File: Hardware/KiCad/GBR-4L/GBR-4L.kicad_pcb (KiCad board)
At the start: 4 copper layers, 160 x 100 mm, 188 parts, among them J1 USB4105-GF-A, J101 EM7565 M.2 Key B socket, J102 MODEM_CONTROL, J201 EM7565 M.2 Key B socket, J202 MODEM_CONTROL, J301 EM7565 M.2 Key B socket, J302 MODEM_CONTROL, J401 EM7565 M.2 Key B socket, J402 MODEM_CONTROL, J511 2452808-1 nano-SIM, J521 2452808-1 nano-SIM, J531 2452808-1 nano-SIM, J541 2452808-1 nano-SIM, J701 12V INPUT 5A, Q701 30V P-MOSFET low-RDS(on), Q911 MMBT3906, Q921 MMBT3906, Q931 MMBT3906, Q941 MMBT3906, SW911 MODEM 1 RESET, SW912 MODEM 1 RF DISABLE, SW921 MODEM 2 RESET, SW922 MODEM 2 RF DISABLE, SW931 MODEM 3 RESET, SW932 MODEM 3 RF DISABLE, SW941 MODEM 4 RESET, SW942 MODEM 4 RF DISABLE, U1 USBLC6-2SC6, U11 LOW-CAP SIM ESD ARRAY, U12 LOW-CAP SIM ESD ARRAY, U13 LOW-CAP SIM ESD ARRAY, U14 LOW-CAP SIM ESD ARRAY, U2 USB2514Bi-I/M2, U21 TPS56339DDCR, U22 TPS56339DDCR, U23 TPS56339DDCR, U24 TPS56339DDCR, U25 TPS56339DDCR, Y1 24MHz

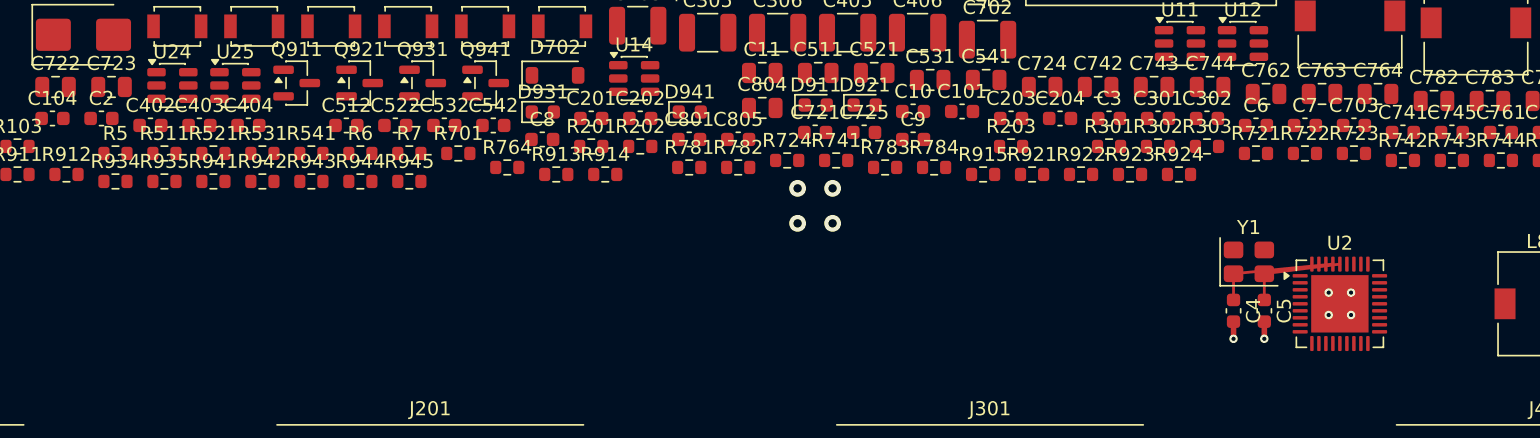
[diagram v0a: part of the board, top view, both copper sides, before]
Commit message: Place and route USB hub filters
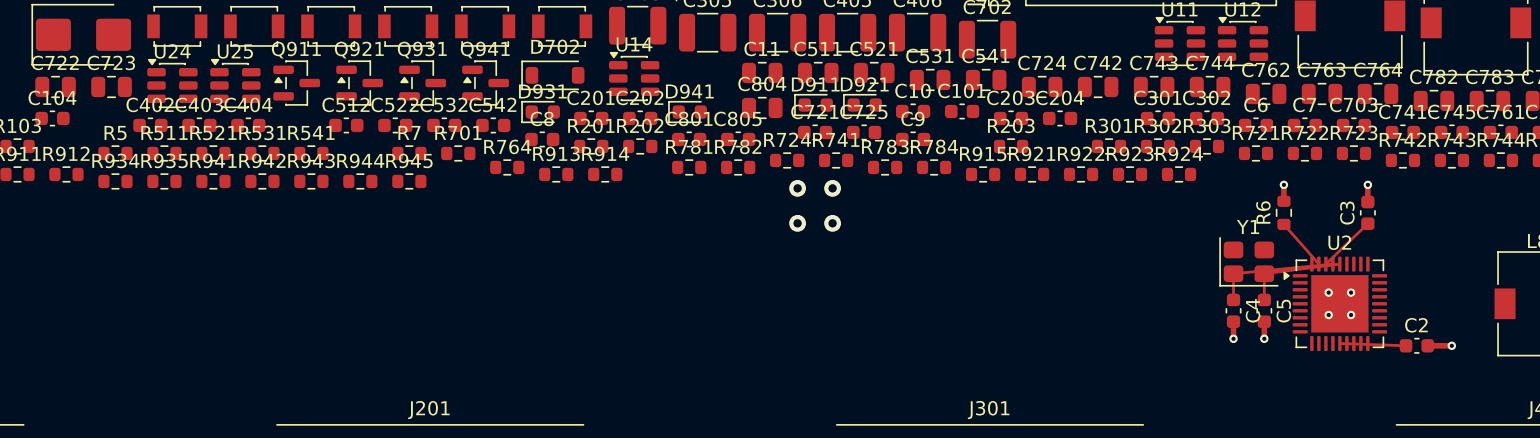
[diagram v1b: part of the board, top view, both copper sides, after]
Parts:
- moved C2 95.4 mm to (150.5, 58.0)
- moved R6 66.1 mm to (141.0, 48.5), turned to 90 degrees
- moved C3 19.7 mm to (147.0, 48.5), turned to 90 degrees
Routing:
- net HUB_CRFILT: track 0.00 -> 4.73 mm
- net HUB_PLLFILT: track 0.00 -> 4.16 mm
- net GND: track 18.0 -> 22.1 mm, vias 57 -> 60
- net HUB_RBIAS: track 0.00 -> 3.78 mm
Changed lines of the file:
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@@
 	(footprint "Capacitor_SMD:C_0603_1608Metric"
 		(layer "F.Cu")
-		(at 56.505 41.754999)
+		(at 150.5 58)
 		(descr "Capacitor SMD 0603 (1608 Metric), square (rectangular) end terminal, IPC-7351 nominal, (Body size source: IPC-SM-782 page 76, https://www.pcb-3d.com/wordpress/wp-content/uploads/ipc-sm-782a_amendment_1_and_2.pdf)")
 		(tags "capacitor")
@@
 	(footprint "Resistor_SMD:R_0603_1608Metric"
 		(layer "F.Cu")
-		(at 75.005 44.255)
+		(at 141 48.5 90)
 		(descr "Resistor SMD 0603 (1608 Metric), square (rectangular) end terminal, IPC-7351 nominal, (Body size source: IPC-SM-782 page 72, https://www.pcb-3d.com/wordpress/wp-content/uploads/ipc-sm-782a_amendment_1_and_2.pdf)")
 		(tags "resistor")
 		(property "Reference" "R6"
-			(at 0 -1.43 0)
+			(at 0 -1.43 90)
 			(layer "F.SilkS")
 			(effects
@@
 		)
 		(property "Value" "12.0k 1%"
-			(at 0 1.43 0)
+			(at 0 1.43 90)
 			(layer "F.Fab")
 			(effects
@@
 		)
 		(property "Datasheet" ""
-			(at 0 0 0)
+			(at 0 0 90)
 			(layer "F.Fab")
 			(hide yes)
@@
 		)
 		(property "Description" ""
-			(at 0 0 0)
+			(at 0 0 90)
 			(layer "F.Fab")
 			(hide yes)
@@
 		)
 		(property "KiLib_Generator" "SMD_2terminal_chip_molded"
-			(at 0 0 0)
+			(at 0 0 90)
 			(layer "F.SilkS")
 			(hide yes)
@@
 		)
 		(fp_text user "${REFERENCE}"
-			(at 0 0 0)
+			(at 0 0 90)
 			(layer "F.Fab")
 			(effects
@@
 		)
 		(pad "1" smd roundrect
-			(at -0.825 0)
+			(at -0.825 0 90)
 			(size 0.8 0.95)
 			(layers "F.Cu" "F.Mask" "F.Paste")
@@
 		)
 		(pad "2" smd roundrect
-			(at 0.825 0)
+			(at 0.825 0 90)
 			(size 0.8 0.95)
 			(layers "F.Cu" "F.Mask" "F.Paste")
@@
 	(footprint "Capacitor_SMD:C_0603_1608Metric"
 		(layer "F.Cu")
-		(at 128.504999 41.754999)
+		(at 147 48.5 90)
 		(descr "Capacitor SMD 0603 (1608 Metric), square (rectangular) end terminal, IPC-7351 nominal, (Body size source: IPC-SM-782 page 76, https://www.pcb-3d.com/wordpress/wp-content/uploads/ipc-sm-782a_amendment_1_and_2.pdf)")
 		(tags "capacitor")
 		(property "Reference" "C3"
-			(at 0 -1.43 0)
+			(at 0 -1.43 90)
 			(layer "F.SilkS")
 			(effects
@@
 		)
 		(property "Value" "100nF"
-			(at 0 1.43 0)
+			(at 0 1.43 90)
 			(layer "F.Fab")
 			(effects
@@
 		)
 		(property "Datasheet" ""
-			(at 0 0 0)
+			(at 0 0 90)
 			(layer "F.Fab")
 			(hide yes)
@@
 		)
 		(property "Description" ""
-			(at 0 0 0)
+			(at 0 0 90)
 			(layer "F.Fab")
 			(hide yes)
@@
 		)
 		(property "KiLib_Generator" "SMD_2terminal_chip_molded"
-			(at 0 0 0)
+			(at 0 0 90)
 			(layer "F.SilkS")
 			(hide yes)
@@
 		)
 		(fp_text user "${REFERENCE}"
-			(at 0 0 0)
+			(at 0 0 90)
 			(layer "F.Fab")
 			(effects
@@
 		)
 		(pad "1" smd roundrect
-			(at -0.775 0)
+			(at -0.775 0 90)
 			(size 0.9 0.95)
 			(layers "F.Cu" "F.Mask" "F.Paste")
@@
 		)
 		(pad "2" smd roundrect
-			(at 0.775 0)
+			(at 0.775 0 90)
 			(size 0.9 0.95)
 			(layers "F.Cu" "F.Mask" "F.Paste")
@@
 	)
 	(segment
+		(start 147 47.725)
+		(end 147 46.5)
+		(width 0.4)
+		(layer "F.Cu")
+		(net "GND")
+	)
+	(segment
+		(start 151.275 58)
+		(end 153 58)
+		(width 0.4)
+		(layer "F.Cu")
+		(net "GND")
+	)
+	(segment
 		(start 171.32 31.8)
 		(end 168.5 31.8)
@@
 		(net "GND")
 	)
+	(segment
+		(start 141 47.675)
+		(end 141 46.5)
+		(width 0.4)
+		(layer "F.Cu")
+		(net "GND")
+	)
 	(via
 		(at 168.5 31.8)
@@
 	)
 	(via
+		(at 153 58)
+		(size 0.6)
+		(drill 0.3)
+		(layers "F.Cu" "B.Cu")
+		(net "GND")
+	)
+	(via
 		(at 139.6 57.5)
 		(size 0.6)
@@
 	)
 	(via
+		(at 147 46.5)
+		(size 0.6)
+		(drill 0.3)
+		(layers "F.Cu" "B.Cu")
+		(net "GND")
+	)
+	(via
 		(at 110 117)
 		(size 0.6)
@@
 	)
 	(via
+		(at 141 46.5)
+		(size 0.6)
+		(drill 0.3)
+		(layers "F.Cu" "B.Cu")
+		(net "GND")
+	)
+	(via
 		(at 170.325 56)
 		(size 0.6)
@@
 	)
 	(segment
+		(start 149.725 58)
+		(end 145 57.8375)
+		(width 0.2)
+		(layer "F.Cu")
+		(net "HUB_CRFILT")
+	)
+	(segment
 		(start 171.9 39.32)
 		(end 168.5 39.32)
@@
 	)
 	(segment
+		(start 141 49.325)
+		(end 143.5 52.1625)
+		(width 0.2)
+		(layer "F.Cu")
+		(net "HUB_RBIAS")
+	)
+	(segment
 		(start 137.4 52.85)
 		(end 137.4 54.725)
@@
 		(net "HUB_XTALIN")
 	)
+	(segment
+		(start 147 49.275)
+		(end 144 52.1625)
+		(width 0.2)
+		(layer "F.Cu")
+		(net "HUB_PLLFILT")
+	)
 	(zone

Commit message: Place and route USB hub decoupling
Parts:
- moved C8 64.0 mm to (151.5, 51.5)
- moved C11 49.7 mm to (148.0, 61.0), turned to -90 degrees
- moved C9 35.3 mm to (145.0, 61.0), turned to -90 degrees
- moved C10 33.9 mm to (142.0, 61.0), turned to -90 degrees
- moved C7 14.8 mm to (151.5, 54.0)
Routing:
- net +3V3_SYS: track 0.00 -> 17.4 mm
- net GND: track 22.1 -> 29.0 mm, vias 60 -> 65
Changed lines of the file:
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@@
 	(footprint "Capacitor_SMD:C_0603_1608Metric"
 		(layer "F.Cu")
-		(at 88.005001 43.254999)
+		(at 151.5 51.5)
 		(descr "Capacitor SMD 0603 (1608 Metric), square (rectangular) end terminal, IPC-7351 nominal, (Body size source: IPC-SM-782 page 76, https://www.pcb-3d.com/wordpress/wp-content/uploads/ipc-sm-782a_amendment_1_and_2.pdf)")
 		(tags "capacitor")
@@
 	(footprint "Capacitor_SMD:C_0603_1608Metric"
 		(layer "F.Cu")
-		(at 114.505 41.254999)
+		(at 142 61 -90)
 		(descr "Capacitor SMD 0603 (1608 Metric), square (rectangular) end terminal, IPC-7351 nominal, (Body size source: IPC-SM-782 page 76, https://www.pcb-3d.com/wordpress/wp-content/uploads/ipc-sm-782a_amendment_1_and_2.pdf)")
 		(tags "capacitor")
 		(property "Reference" "C10"
-			(at 0 -1.43 0)
+			(at 0 -1.43 270)
 			(layer "F.SilkS")
 			(effects
@@
 		)
 		(property "Value" "100nF"
-			(at 0 1.43 0)
+			(at 0 1.43 270)
 			(layer "F.Fab")
 			(effects
@@
 		)
 		(property "Datasheet" ""
-			(at 0 0 0)
+			(at 0 0 270)
 			(layer "F.Fab")
 			(hide yes)
@@
 		)
 		(property "Description" ""
-			(at 0 0 0)
+			(at 0 0 270)
 			(layer "F.Fab")
 			(hide yes)
@@
 		)
 		(property "KiLib_Generator" "SMD_2terminal_chip_molded"
-			(at 0 0 0)
+			(at 0 0 270)
 			(layer "F.SilkS")
 			(hide yes)
@@
 		(duplicate_pad_numbers_are_jumpers no)
 		(fp_line
-			(start -0.14058 -0.51)
-			(end 0.14058 -0.51)
+			(start -0.14058 0.51)
+			(end 0.14058 0.51)
 			(stroke
 				(width 0.12)
@@
 		)
 		(fp_line
-			(start -0.14058 0.51)
-			(end 0.14058 0.51)
+			(start -0.14058 -0.51)
+			(end 0.14058 -0.51)
 			(stroke
 				(width 0.12)
@@
 		)
 		(fp_text user "${REFERENCE}"
-			(at 0 0 0)
+			(at 0 0 270)
 			(layer "F.Fab")
 			(effects
@@
 		)
 		(pad "1" smd roundrect
-			(at -0.775 0)
+			(at -0.775 0 270)
 			(size 0.9 0.95)
 			(layers "F.Cu" "F.Mask" "F.Paste")
@@
 		)
 		(pad "2" smd roundrect
-			(at 0.775 0)
+			(at 0.775 0 270)
 			(size 0.9 0.95)
 			(layers "F.Cu" "F.Mask" "F.Paste")
@@
 	(footprint "Capacitor_SMD:C_0603_1608Metric"
 		(layer "F.Cu")
-		(at 142.505 42.254999)
+		(at 151.5 54)
 		(descr "Capacitor SMD 0603 (1608 Metric), square (rectangular) end terminal, IPC-7351 nominal, (Body size source: IPC-SM-782 page 76, https://www.pcb-3d.com/wordpress/wp-content/uploads/ipc-sm-782a_amendment_1_and_2.pdf)")
 		(tags "capacitor")
@@
 	(footprint "Capacitor_SMD:C_0805_2012Metric"
 		(layer "F.Cu")
-		(at 103.725 38.505)
+		(at 148 61 -90)
 		(descr "Capacitor SMD 0805 (2012 Metric), square (rectangular) end terminal, IPC-7351 nominal, (Body size source: IPC-SM-782 page 76, https://www.pcb-3d.com/wordpress/wp-content/uploads/ipc-sm-782a_amendment_1_and_2.pdf, https://docs.google.com/spreadsheets/d/1BsfQQcO9C6DZCsRaXUlFlo91Tg2WpOkGARC1WS5S8t0/edit?usp=sharing)")
 		(tags "capacitor")
 		(property "Reference" "C11"
-			(at 0 -1.68 0)
+			(at 0 -1.68 270)
 			(layer "F.SilkS")
 			(effects
@@
 		)
 		(property "Value" "4.7uF"
-			(at 0 1.68 0)
+			(at 0 1.68 270)
 			(layer "F.Fab")
 			(effects
@@
 		)
 		(property "Datasheet" ""
-			(at 0 0 0)
+			(at 0 0 270)
 			(layer "F.Fab")
 			(hide yes)
@@
 		)
 		(property "Description" ""
-			(at 0 0 0)
+			(at 0 0 270)
 			(layer "F.Fab")
 			(hide yes)
@@
 		)
 		(property "KiLib_Generator" "SMD_2terminal_chip_molded"
-			(at 0 0 0)
+			(at 0 0 270)
 			(layer "F.SilkS")
 			(hide yes)
@@
 		(duplicate_pad_numbers_are_jumpers no)
 		(fp_line
-			(start -0.261252 -0.735)
-			(end 0.261252 -0.735)
+			(start -0.261252 0.735)
+			(end 0.261252 0.735)
 			(stroke
 				(width 0.12)
@@
 		)
 		(fp_line
-			(start -0.261252 0.735)
-			(end 0.261252 0.735)
+			(start -0.261252 -0.735)
+			(end 0.261252 -0.735)
 			(stroke
 				(width 0.12)
@@
 		)
 		(fp_text user "${REFERENCE}"
-			(at 0 0 0)
+			(at 0 0 270)
 			(layer "F.Fab")
 			(effects
@@
 		)
 		(pad "1" smd roundrect
-			(at -0.95 0)
+			(at -0.95 0 270)
 			(size 1 1.45)
 			(layers "F.Cu" "F.Mask" "F.Paste")
@@
 		)
 		(pad "2" smd roundrect
-			(at 0.95 0)
+			(at 0.95 0 270)
 			(size 1 1.45)
 			(layers "F.Cu" "F.Mask" "F.Paste")
@@
 	(footprint "Capacitor_SMD:C_0603_1608Metric"
 		(layer "F.Cu")
-		(at 114.505 43.254999)
+		(at 145 61 -90)
 		(descr "Capacitor SMD 0603 (1608 Metric), square (rectangular) end terminal, IPC-7351 nominal, (Body size source: IPC-SM-782 page 76, https://www.pcb-3d.com/wordpress/wp-content/uploads/ipc-sm-782a_amendment_1_and_2.pdf)")
 		(tags "capacitor")
 		(property "Reference" "C9"
-			(at 0 -1.43 0)
+			(at 0 -1.43 270)
 			(layer "F.SilkS")
 			(effects
@@
 		)
 		(property "Value" "100nF"
-			(at 0 1.43 0)
+			(at 0 1.43 270)
 			(layer "F.Fab")
 			(effects
@@
 		)
 		(property "Datasheet" ""
-			(at 0 0 0)
+			(at 0 0 270)
 			(layer "F.Fab")
 			(hide yes)
@@
 		)
 		(property "Description" ""
-			(at 0 0 0)
+			(at 0 0 270)
 			(layer "F.Fab")
 			(hide yes)
@@
 		)
 		(property "KiLib_Generator" "SMD_2terminal_chip_molded"
-			(at 0 0 0)
+			(at 0 0 270)
 			(layer "F.SilkS")
 			(hide yes)
@@
 		(duplicate_pad_numbers_are_jumpers no)
 		(fp_line
-			(start -0.14058 -0.51)
-			(end 0.14058 -0.51)
+			(start -0.14058 0.51)
+			(end 0.14058 0.51)
 			(stroke
 				(width 0.12)
@@
 		)
 		(fp_line
-			(start -0.14058 0.51)
-			(end 0.14058 0.51)
+			(start -0.14058 -0.51)
+			(end 0.14058 -0.51)
 			(stroke
 				(width 0.12)
@@
 		)
 		(fp_text user "${REFERENCE}"
-			(at 0 0 0)
+			(at 0 0 270)
 			(layer "F.Fab")
 			(effects
@@
 		)
 		(pad "1" smd roundrect
-			(at -0.775 0)
+			(at -0.775 0 270)
 			(size 0.9 0.95)
 			(layers "F.Cu" "F.Mask" "F.Paste")
@@
 		)
 		(pad "2" smd roundrect
-			(at 0.775 0)
+			(at 0.775 0 270)
 			(size 0.9 0.95)
 			(layers "F.Cu" "F.Mask" "F.Paste")
@@
 	)
 	(segment
+		(start 145 61.775)
+		(end 145 63)
+		(width 0.4)
+		(layer "F.Cu")
+		(net "GND")
+	)
+	(segment
 		(start 177 47.025)
 		(end 179 47.025)
@@
 	)
 	(segment
+		(start 142 61.775)
+		(end 142 63)
+		(width 0.4)
+		(layer "F.Cu")
+		(net "GND")
+	)
+	(segment
 		(start 137.4 56.275)
 		(end 137.4 57.5)
@@
 	)
 	(segment
+		(start 152.275 51.5)
+		(end 154 51.5)
+		(width 0.4)
+		(layer "F.Cu")
+		(net "GND")
+	)
+	(segment
 		(start 151.275 58)
 		(end 153 58)
@@
 	)
 	(segment
+		(start 152.275 54)
+		(end 154 54)
+		(width 0.4)
+		(layer "F.Cu")
+		(net "GND")
+	)
+	(segment
 		(start 141 47.675)
 		(end 141 46.5)
@@
 		(net "GND")
 	)
+	(segment
+		(start 148 61.95)
+		(end 148 63)
+		(width 0.4)
+		(layer "F.Cu")
+		(net "GND")
+	)
 	(via
 		(at 168.5 31.8)
@@
 	)
 	(via
+		(at 142 63)
+		(size 0.6)
+		(drill 0.3)
+		(layers "F.Cu" "B.Cu")
+		(net "GND")
+	)
+	(via
 		(at 153 58)
 		(size 0.6)
@@
 	)
 	(via
+		(at 148 63)
+		(size 0.6)
+		(drill 0.3)
+		(layers "F.Cu" "B.Cu")
+		(net "GND")
+	)
+	(via
 		(at 145.8 55.8)
 		(size 0.6)
@@
 	)
 	(via
+		(at 145 63)
+		(size 0.6)
+		(drill 0.3)
+		(layers "F.Cu" "B.Cu")
+		(net "GND")
+	)
+	(via
 		(at 23 70)
 		(size 0.6)
@@
 	)
 	(via
+		(at 154 54)
+		(size 0.6)
+		(drill 0.3)
+		(layers "F.Cu" "B.Cu")
+		(net "GND")
+	)
+	(via
 		(at 35 75)
 		(size 0.6)
@@
 	)
 	(via
+		(at 154 51.5)
+		(size 0.6)
+		(drill 0.3)
+		(layers "F.Cu" "B.Cu")
+		(net "GND")
+	)
+	(via
 		(at 23 100)
 		(size 0.6)
@@
 		(net "+3V3_M3")
 	)
+	(segment
+		(start 150.725 51.5)
+		(end 146.5 52.1625)
+		(width 0.4)
+		(layer "F.Cu")
+		(net "+3V3_SYS")
+	)
+	(segment
+		(start 145 60.225)
+		(end 145.5 57.8375)
+		(width 0.4)
+		(layer "F.Cu")
+		(net "+3V3_SYS")
+	)
+	(segment
+		(start 148 60.05)
+		(end 147.8375 55)
+		(width 0.4)
+		(layer "F.Cu")
+		(net "+3V3_SYS")
+	)
+	(segment
+		(start 150.725 54)
+		(end 147.8375 55)
+		(width 0.4)
+		(layer "F.Cu")
+		(net "+3V3_SYS")
+	)
+	(segment
+		(start 142 60.225)
+		(end 143 57.8375)
+		(width 0.4)
+		(layer "F.Cu")
+		(net "+3V3_SYS")
+	)
 	(via

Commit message: Connect USB hub to system power plane
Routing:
- net +3V3_SYS: track 17.4 -> 27.4 mm, vias 4 -> 6
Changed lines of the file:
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@@
+	)
+	(segment
+		(start 134 59.5)
+		(end 134 61.5)
+		(width 1)
+		(layer "F.Cu")
+		(net "+3V3_SYS")
 	)
 	(segment
@@
 		(end 147.8375 55)
 		(width 0.4)
+		(layer "F.Cu")
+		(net "+3V3_SYS")
+	)
+	(segment
+		(start 134 59.5)
+		(end 142 60.225)
+		(width 1)
 		(layer "F.Cu")
 		(net "+3V3_SYS")
@@
 		(size 1.2)
 		(drill 0.6)
+		(layers "F.Cu" "B.Cu")
+		(net "+3V3_SYS")
+	)
+	(via
+		(at 134 59.5)
+		(size 1.2)
+		(drill 0.6)
+		(layers "F.Cu" "B.Cu")
+		(net "+3V3_SYS")
+	)
+	(via
+		(at 134 61.5)
+		(size 1.2)
+		(drill 0.6)

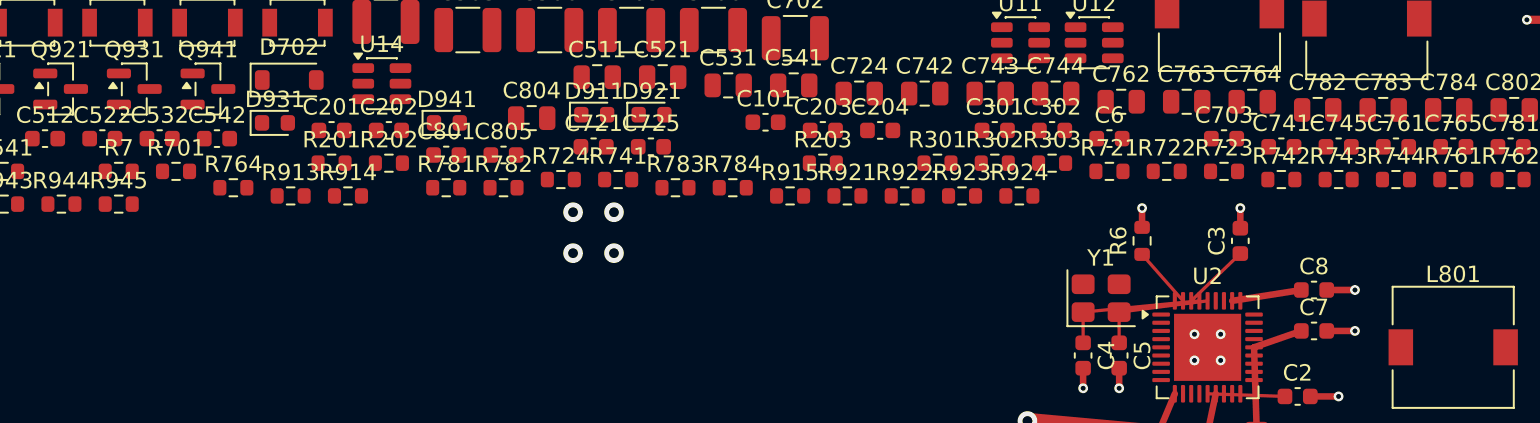
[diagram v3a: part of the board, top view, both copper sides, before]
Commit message: Place and route USB hub reset network
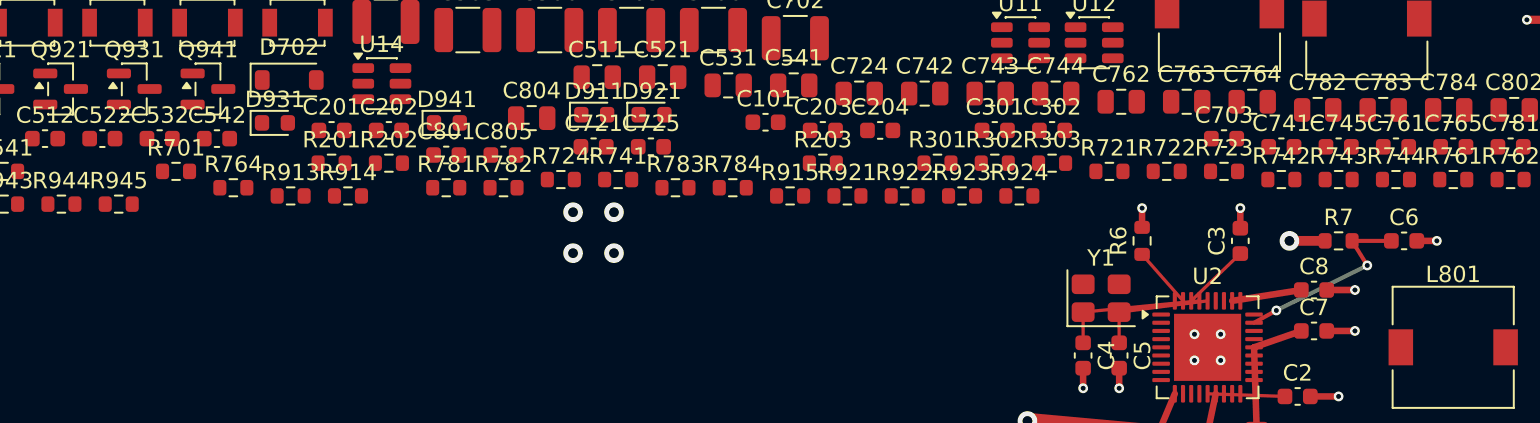
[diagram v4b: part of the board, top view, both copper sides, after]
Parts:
- moved R7 74.6 mm to (153.0, 48.5)
- moved C6 19.0 mm to (157.0, 48.5)
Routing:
- net HUB_RESET#: track 0.00 -> 11.9 mm, vias 0 -> 2
- net +3V3_SYS: track 27.4 -> 29.6 mm, vias 6 -> 7
- net GND: track 29.0 -> 30.3 mm, vias 65 -> 66
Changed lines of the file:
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@@
 	(footprint "Resistor_SMD:R_0603_1608Metric"
 		(layer "F.Cu")
-		(at 78.505 44.254999)
+		(at 153 48.5)
 		(descr "Resistor SMD 0603 (1608 Metric), square (rectangular) end terminal, IPC-7351 nominal, (Body size source: IPC-SM-782 page 72, https://www.pcb-3d.com/wordpress/wp-content/uploads/ipc-sm-782a_amendment_1_and_2.pdf)")
 		(tags "resistor")
@@
 	(footprint "Capacitor_SMD:C_0603_1608Metric"
 		(layer "F.Cu")
-		(at 139.005 42.254999)
+		(at 157 48.5)
 		(descr "Capacitor SMD 0603 (1608 Metric), square (rectangular) end terminal, IPC-7351 nominal, (Body size source: IPC-SM-782 page 76, https://www.pcb-3d.com/wordpress/wp-content/uploads/ipc-sm-782a_amendment_1_and_2.pdf)")
 		(tags "capacitor")
@@
 	)
 	(segment
+		(start 157.775 48.5)
+		(end 159 48.5)
+		(width 0.4)
+		(layer "F.Cu")
+		(net "GND")
+	)
+	(segment
 		(start 174.325 54)
 		(end 174.325 56)
@@
 	)
 	(via
+		(at 159 48.5)
+		(size 0.6)
+		(drill 0.3)
+		(layers "F.Cu" "B.Cu")
+		(net "GND")
+	)
+	(via
 		(at 85 75)
 		(size 0.6)
@@
 	)
 	(segment
+		(start 152.175 48.5)
+		(end 150 48.5)
+		(width 0.6)
+		(layer "F.Cu")
+		(net "+3V3_SYS")
+	)
+	(segment
 		(start 148 60.05)
 		(end 147.8375 55)
@@
 	)
 	(via
+		(at 150 48.5)
+		(size 1.2)
+		(drill 0.6)
+		(layers "F.Cu" "B.Cu")
+		(net "+3V3_SYS")
+	)
+	(via
 		(at 106.25 46.75)
 		(size 1.2)
@@
 	)
 	(segment
+		(start 147.8375 53.5)
+		(end 149.2 52.75)
+		(width 0.25)
+		(layer "F.Cu")
+		(net "HUB_RESET#")
+	)
+	(segment
+		(start 153.825 48.5)
+		(end 156.225 48.5)
+		(width 0.25)
+		(layer "F.Cu")
+		(net "HUB_RESET#")
+	)
+	(segment
+		(start 153.825 48.5)
+		(end 154.75 50)
+		(width 0.25)
+		(layer "F.Cu")
+		(net "HUB_RESET#")
+	)
+	(via
+		(at 154.75 50)
+		(size 0.6)
+		(drill 0.3)
+		(layers "F.Cu" "B.Cu")
+		(net "HUB_RESET#")
+	)
+	(via
+		(at 149.2 52.75)
+		(size 0.6)
+		(drill 0.3)
+		(layers "F.Cu" "B.Cu")
+		(net "HUB_RESET#")
+	)
+	(segment
+		(start 149.2 52.75)
+		(end 154.75 50)
+		(width 0.25)
+		(layer "B.Cu")
+		(net "HUB_RESET#")
+	)
+	(segment
